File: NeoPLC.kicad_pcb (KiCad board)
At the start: 2 copper layers, 0 parts

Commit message: DI-8 şema ve PCB taslağı: platform kararları kilitlendi, çekirdek/saha yerleşimi GitHub’da.
Birkaç saatlik stabil anlarda origin’e push kuralı eklendi; yerel KiCAD geçmişi ve Konnect önizlemeleri commit dışı bırakıldı.

Co-authored-by: Cursor <cursoragent@cursor.com>
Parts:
- added C1: 10uF, Capacitor_SMD:C_0805_2012Metric, F.Cu at (12.0, 14.0)
- added C2: 100nF, Capacitor_SMD:C_0402_1005Metric, F.Cu at (15.0, 14.0)
- added C3: 10uF, Capacitor_SMD:C_0805_2012Metric, F.Cu at (24.5, 14.0)
- added C4: 100nF, Capacitor_SMD:C_0402_1005Metric, F.Cu at (21.0, 14.0)
- added C5: 100nF, Capacitor_SMD:C_0402_1005Metric, F.Cu at (20.5, 29.5)
- added C6: 100nF, Capacitor_SMD:C_0402_1005Metric, F.Cu at (20.5, 32.0)
- added C7: 100nF, Capacitor_SMD:C_0402_1005Metric, F.Cu at (20.5, 34.5)
- added C8: 15pF, Capacitor_SMD:C_0402_1005Metric, F.Cu at (17.0, 30.0)
- added C9: 15pF, Capacitor_SMD:C_0402_1005Metric, F.Cu at (17.0, 37.0)
- added D1: LED, LED_SMD:LED_0805_2012Metric, F.Cu at (10.0, 42.0)
- added J1: Backplane 2x6, NeoPLC:GoldFinger_2x6_2.54, F.Cu at (37.5, 0.00)
- added J2: DI1-4+COM 3.5mm, Connector_Phoenix_MC:PhoenixContact_MCV_1,5_5-G-3.5_1x05_P3.50mm_Vertical, F.Cu at (21.0, 105.0)
- added J3: DI5-8+COM 3.5mm, Connector_Phoenix_MC:PhoenixContact_MCV_1,5_5-G-3.5_1x05_P3.50mm_Vertical, F.Cu at (68.0, 105.0)
- added J4: SWD, Connector_PinHeader_2.54mm:PinHeader_1x05_P2.54mm_Vertical, F.Cu at (63.0, 22.0)
- added R1: 10k, Resistor_SMD:R_0402_1005Metric, F.Cu at (20.5, 38.5)
- added R10: 3.3k, Resistor_SMD:R_1206_3216Metric, F.Cu at (62.0, 86.0)
- added R11: 3.3k, Resistor_SMD:R_1206_3216Metric, F.Cu at (64.5, 86.0)
- added R12: 10k, Resistor_SMD:R_0402_1005Metric, F.Cu at (11.5, 67.0)
- added R13: 10k, Resistor_SMD:R_0402_1005Metric, F.Cu at (14.0, 67.0)
- added R14: 10k, Resistor_SMD:R_0402_1005Metric, F.Cu at (16.5, 67.0)
- added R15: 10k, Resistor_SMD:R_0402_1005Metric, F.Cu at (19.0, 67.0)
- added R16: 10k, Resistor_SMD:R_0402_1005Metric, F.Cu at (57.0, 67.0)
- added R17: 10k, Resistor_SMD:R_0402_1005Metric, F.Cu at (59.5, 67.0)
- added R18: 10k, Resistor_SMD:R_0402_1005Metric, F.Cu at (62.0, 67.0)
- added R19: 10k, Resistor_SMD:R_0402_1005Metric, F.Cu at (64.5, 67.0)
- added R2: 1k, Resistor_SMD:R_0402_1005Metric, F.Cu at (10.0, 38.5)
- added R3: 1M, Resistor_SMD:R_0402_1005Metric, F.Cu at (13.5, 33.5)
- added R4: 3.3k, Resistor_SMD:R_1206_3216Metric, F.Cu at (11.5, 86.0)
- added R5: 3.3k, Resistor_SMD:R_1206_3216Metric, F.Cu at (14.0, 86.0)
- added R6: 3.3k, Resistor_SMD:R_1206_3216Metric, F.Cu at (16.5, 86.0)
- added R7: 3.3k, Resistor_SMD:R_1206_3216Metric, F.Cu at (19.0, 86.0)
- added R8: 3.3k, Resistor_SMD:R_1206_3216Metric, F.Cu at (57.0, 86.0)
- added R9: 3.3k, Resistor_SMD:R_1206_3216Metric, F.Cu at (59.5, 86.0)
- added U1: STM32G071CBT6, Package_QFP:LQFP-48_7x7mm_P0.5mm, F.Cu at (28.0, 32.0)
- added U2: AP2112K-3.3, Package_TO_SOT_SMD:SOT-23-5, F.Cu at (18.0, 14.0)
- added U3: ISL3178EIBZ, Package_SO:SOIC-8_3.9x4.9mm_P1.27mm, F.Cu at (52.0, 16.0)
- added U4: TLP291-4, Package_SO:SOIC-16_4.55x10.3mm_P1.27mm, F.Cu at (16.0, 74.0)
- added U5: TLP291-4, Package_SO:SOIC-16_4.55x10.3mm_P1.27mm, F.Cu at (61.5, 74.0)
- added Y1: 8MHz, Crystal:Crystal_SMD_3225-4Pin_3.2x2.5mm, F.Cu at (17.0, 33.5)
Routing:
- net +3V3: track 0.00 -> 296.0 mm, vias 0 -> 13
- net /Node Core/MOD_RST#: track 0.00 -> 214.9 mm, vias 0 -> 13
- net /DI Field/FIELD_COM: track 0.00 -> 124.9 mm
- net /DI Field/DI5: track 0.00 -> 83.7 mm, vias 0 -> 12
- net /DI Field/DI6: track 0.00 -> 81.8 mm, vias 0 -> 13
- net /DI Field/DI7: track 0.00 -> 80.0 mm, vias 0 -> 12
- net /DI Field/DI8: track 0.00 -> 78.2 mm, vias 0 -> 11
- net GND: track 0.00 -> 59.4 mm, vias 0 -> 6
- net /DI Field/DI2: track 0.00 -> 55.5 mm, vias 0 -> 8
- net /Node Core/SWDIO: track 0.00 -> 50.0 mm, vias 0 -> 2
- net /DI Field/DI1: track 0.00 -> 48.8 mm, vias 0 -> 10
- net /DI Field/DI4: track 0.00 -> 47.3 mm, vias 0 -> 11
- net /Node Core/SWCLK: track 0.00 -> 47.0 mm, vias 0 -> 2
- net /Node Core/STATUS_LED: track 0.00 -> 43.5 mm, vias 0 -> 5
- net /DI Field/DI3: track 0.00 -> 43.2 mm, vias 0 -> 8
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- added copper zone on F.Cu, net /DI Field/FIELD_COM
- added copper zone on B.Cu, net GND
- added copper zone on F.Cu, net GND
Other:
- board outline added: 75 x 110 mm

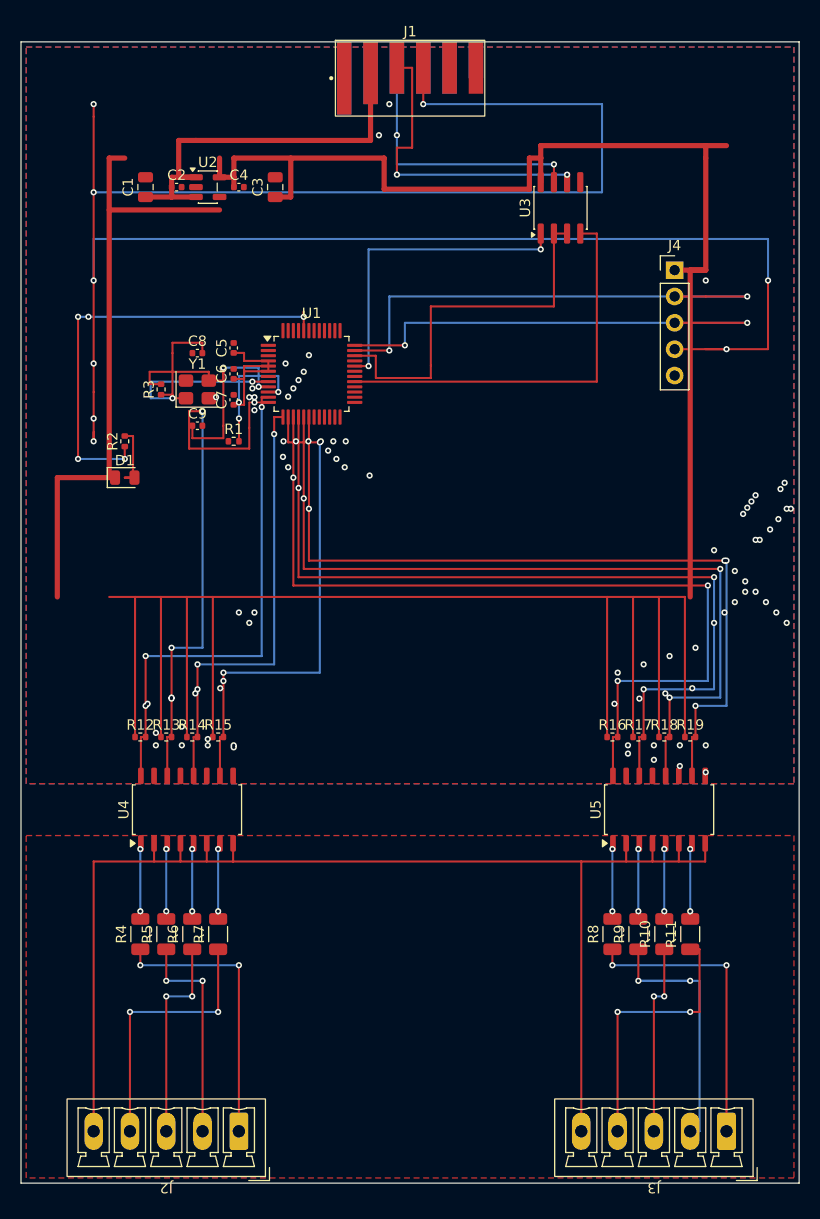
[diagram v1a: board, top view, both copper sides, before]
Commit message: DI6/DI4 last-mile ve J1 +5V arka pad: MCU’ya bakır kapandı, DRC 134→101.
Co-authored-by: Cursor <cursoragent@cursor.com>
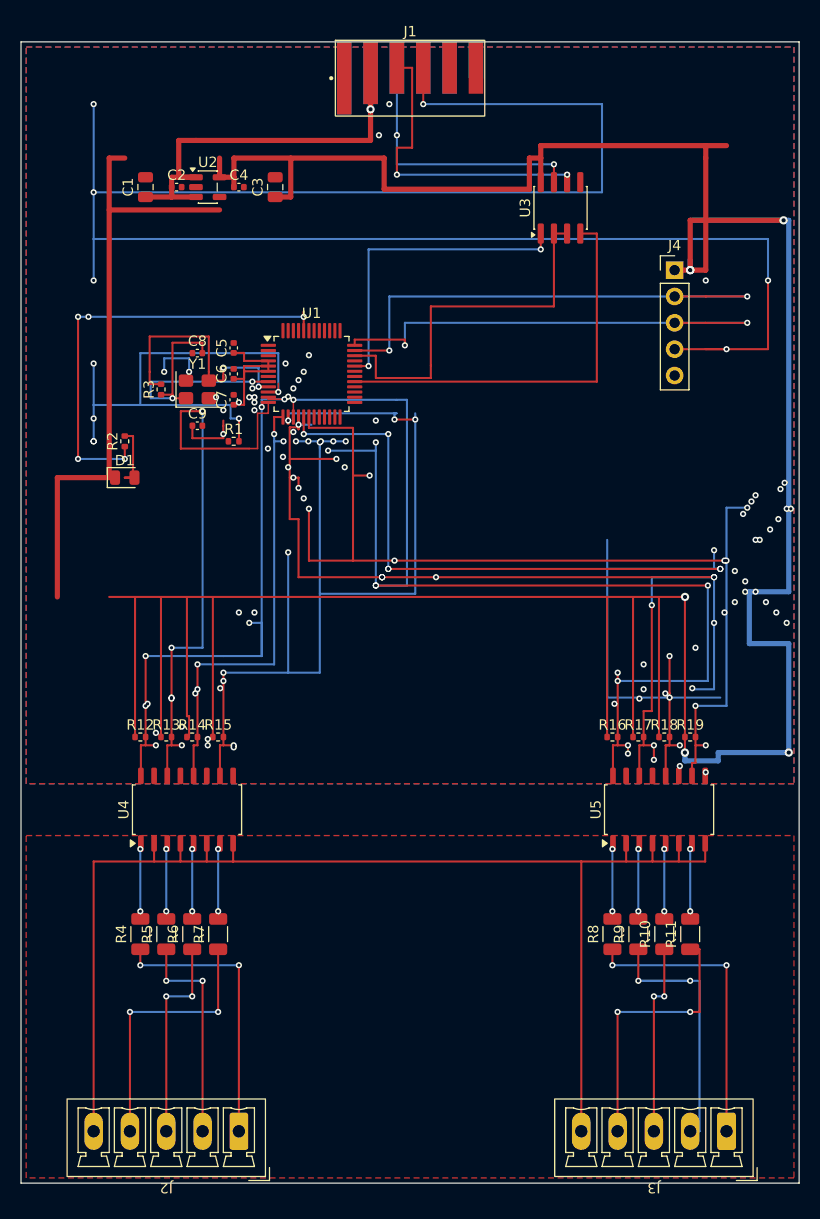
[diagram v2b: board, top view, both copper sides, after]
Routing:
- net +3V3: track 296.0 -> 359.8 mm, vias 13 -> 22
- net /DI Field/DI4: track 47.3 -> 100.8 mm, vias 11 -> 16
- net /DI Field/DI5: track 83.7 -> 114.0 mm, vias 12 -> 14
- net /DI Field/DI7: track 80.0 -> 107.9 mm, vias 12 -> 20
- net /DI Field/DI6: track 81.8 -> 106.9 mm, vias 13 -> 21
- net /DI Field/DI8: track 78.2 -> 97.3 mm, vias 11 -> 10
- net /Node Core/MOD_RST#: track 214.9 -> 230.7 mm, vias 13 -> 14
- net /DI Field/DI1: track 48.8 -> 57.3 mm, vias 10 -> 9
- net GND: track 59.4 -> 64.4 mm, vias 6 -> 8
- net +5V: track 39.3 -> 42.8 mm, vias 0 -> 1
- net /DI Field/DI2: track 55.5 -> 58.1 mm, vias 8 -> 10
- net /Node Core/HSE_OUT: track 28.7 -> 30.8 mm, vias 3 -> 4
- net /Node Core/SWCLK: track 47.0 -> 48.1 mm
- net /DI Field/DI3: track 43.2 -> 44.1 mm

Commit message: +3V3 LDO–MCU köprüsü ve RST/DI ada dikişleri: DRC 98→83.
Co-authored-by: Cursor <cursoragent@cursor.com>
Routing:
- net +3V3: track 359.8 -> 396.7 mm
- net /Node Core/MOD_RST#: track 230.7 -> 248.7 mm, vias 14 -> 13
- net /Node Core/BUS_A: track 30.4 -> 40.1 mm, vias 2 -> 3
- net /Node Core/HSE_OUT: track 30.8 -> 34.7 mm, vias 4 -> 5
- net /DI Field/DI6: track 106.9 -> 110.1 mm
- net /DI Field/DI2: track 58.1 -> 60.1 mm
- net /DI Field/DI7: track 107.9 -> 109.5 mm
- net /DI Field/DI3: track 44.1 -> 45.7 mm
- net /DI Field/DI1: vias 9 -> 8
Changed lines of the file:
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@@
 	)
 	(segment
+		(start 68.8 53.5)
+		(end 68.8 54)
+		(width 0.2)
+		(layer "F.Cu")
+		(net "+3V3")
+	)
+	(segment
 		(start 20.5 32.479999)
 		(end 21.5 32.479999)
@@
 	)
 	(segment
+		(start 71.8 54)
+		(end 71.8 55)
+		(width 0.2)
+		(layer "F.Cu")
+		(net "+3V3")
+	)
+	(segment
 		(start 64.5 17.2)
 		(end 73.5 17.2)
@@
 	)
 	(segment
+		(start 20.52 16)
+		(end 20.52 14)
+		(width 0.5)
+		(layer "F.Cu")
+		(net "+3V3")
+	)
+	(segment
 		(start 66 11.2)
 		(end 66 22)
@@
 	)
 	(segment
+		(start 21.5 16)
+		(end 20.52 16)
+		(width 0.5)
+		(layer "F.Cu")
+		(net "+3V3")
+	)
+	(segment
 		(start 19.1375 13.05)
 		(end 19.1375 11.2)
@@
 	)
 	(segment
+		(start 71.8 55)
+		(end 72.8 55)
+		(width 0.2)
+		(layer "F.Cu")
+		(net "+3V3")
+	)
+	(segment
 		(start 16.2 67)
 		(end 15.99 67)
@@
 	)
 	(segment
+		(start 70.8 54)
+		(end 71.8 54)
+		(width 0.2)
+		(layer "F.Cu")
+		(net "+3V3")
+	)
+	(segment
 		(start 21.5 29.98)
 		(end 21.5 30.75)
@@
 	)
 	(segment
+		(start 21 53.5)
+		(end 21 55)
+		(width 0.5)
+		(layer "F.Cu")
+		(net "+3V3")
+	)
+	(segment
 		(start 63.99 68.5)
 		(end 63.99 67)
@@
 	)
 	(segment
+		(start 34.5 9)
+		(end 34.5 11.2)
+		(width 0.5)
+		(layer "F.Cu")
+		(net "+3V3")
+	)
+	(segment
 		(start 20.52 13.05)
 		(end 20.52 14)
@@
 	)
 	(segment
+		(start 72.8 56)
+		(end 73.8 56)
+		(width 0.2)
+		(layer "F.Cu")
+		(net "+3V3")
+	)
+	(segment
+		(start 21 55)
+		(end 22.5 55)
+		(width 0.5)
+		(layer "F.Cu")
+		(net "+3V3")
+	)
+	(segment
 		(start 66 10)
 		(end 66 11.2)
@@
 	)
 	(segment
+		(start 69.8 53)
+		(end 70.8 53)
+		(width 0.2)
+		(layer "F.Cu")
+		(net "+3V3")
+	)
+	(segment
 		(start 8.5 53.5)
 		(end 64 53.5)
@@
 	)
 	(segment
+		(start 72.8 55)
+		(end 72.8 56)
+		(width 0.2)
+		(layer "F.Cu")
+		(net "+3V3")
+	)
+	(segment
 		(start 66 22)
 		(end 63 22)
@@
 	)
 	(segment
+		(start 70.8 53)
+		(end 70.8 54)
+		(width 0.2)
+		(layer "F.Cu")
+		(net "+3V3")
+	)
+	(segment
 		(start 10.99 53.5)
 		(end 10.99 67)
@@
 	)
 	(segment
+		(start 64 53.5)
+		(end 68.8 53.5)
+		(width 0.2)
+		(layer "F.Cu")
+		(net "+3V3")
+	)
+	(segment
 		(start 23.8375 31.25)
 		(end 23.8375 31.75)
@@
 	)
 	(segment
+		(start 69.8 54)
+		(end 69.8 53)
+		(width 0.2)
+		(layer "F.Cu")
+		(net "+3V3")
+	)
+	(segment
+		(start 21.5 29.98)
+		(end 21.5 16)
+		(width 0.5)
+		(layer "F.Cu")
+		(net "+3V3")
+	)
+	(segment
 		(start 23.8375 30.75)
 		(end 23.8375 31.25)
@@
 	)
 	(segment
+		(start 34.5 11.2)
+		(end 35 11.2)
+		(width 0.5)
+		(layer "F.Cu")
+		(net "+3V3")
+	)
+	(segment
 		(start 64.5 22)
 		(end 64.5 17.2)
@@
 	)
 	(segment
+		(start 68.8 54)
+		(end 69.8 54)
+		(width 0.2)
+		(layer "F.Cu")
+		(net "+3V3")
+	)
+	(segment
 		(start 15.99 65)
 		(end 16.2 65)
@@
 	)
 	(segment
+		(start 14.51 67)
+		(end 14.51 66)
+		(width 0.2)
+		(layer "F.Cu")
+		(net "/DI Field/DI2")
+	)
+	(segment
 		(start 22.8 35.8)
 		(end 23.8375 35.8)
@@
 	)
 	(segment
+		(start 14.51 66)
+		(end 15.5 66)
+		(width 0.2)
+		(layer "F.Cu")
+		(net "/DI Field/DI2")
+	)
+	(segment
 		(start 23.8375 35.8)
 		(end 23.8375 34.75)
@@
 	)
 	(segment
+		(start 19.5 32.65)
+		(end 19.5 36.5)
+		(width 0.2)
+		(layer "F.Cu")
+		(net "/Node Core/HSE_OUT")
+	)
+	(segment
 		(start 19.5 36.5)
 		(end 19.5 37)
@@
 	)
 	(via
+		(at 19.5 35.5)
+		(size 0.6)
+		(drill 0.3)
+		(layers "F.Cu" "B.Cu")
+		(net "/Node Core/HSE_OUT")
+	)
+	(via
 		(at 19.5 37.8)
 		(size 0.6)
@@
 	)
 	(segment
+		(start 25.3 38.5)
+		(end 25.3 40)
+		(width 0.2)
+		(layer "B.Cu")
+		(net "/DI Field/DI3")
+	)
+	(segment
+		(start 25.3 40)
+		(end 25.25 40)
+		(width 0.2)
+		(layer "B.Cu")
+		(net "/DI Field/DI3")
+	)
+	(segment
 		(start 58.325 79)
 		(end 58.325 77.25)
@@
 	)
 	(segment
+		(start 68.8 50.8)
+		(end 68.8 51)
+		(width 0.2)
+		(layer "F.Cu")
+		(net "/DI Field/DI7")
+	)
+	(segment
 		(start 27.25 37.8)
 		(end 27.25 36.1625)
@@
 	)
 	(segment
+		(start 67.4 50.8)
+		(end 68.8 50.8)
+		(width 0.2)
+		(layer "F.Cu")
+		(net "/DI Field/DI7")
+	)
+	(segment
 		(start 62.51 67.8)
 		(end 62.51 67)
@@
 	)
 	(segment
+		(start 60.01 62.4)
+		(end 60.01 60)
+		(width 0.2)
+		(layer "F.Cu")
+		(net "/DI Field/DI6")
+	)
+	(segment
 		(start 25.9 42)
 		(end 26.25 42)
@@
 	)
 	(segment
+		(start 60.01 62.4)
+		(end 60.8 62.4)
+		(width 0.2)
+		(layer "F.Cu")
+		(net "/DI Field/DI6")
+	)
+	(segment
 		(start 60.01 64.5)
 		(end 60.8 64.5)
@@
 	)
 	(via
-		(at 35.5 6)
-		(size 0.6)
-		(drill 0.3)
-		(layers "F.Cu" "B.Cu")
-		(net "/Node Core/MOD_RST#")
-	)
-	(via
 		(at 7 14.5)
 		(size 0.6)
@@
 	)
 	(segment
+		(start 66 23)
+		(end 66 19)
+		(width 0.2)
+		(layer "B.Cu")
+		(net "/Node Core/MOD_RST#")
+	)
+	(segment
 		(start 7 23)
 		(end 7 19)
@@
 	)
 	(segment
+		(start 4 31)
+		(end 7 31)
+		(width 0.2)
+		(layer "B.Cu")
+		(net "/Node Core/MOD_RST#")
+	)
+	(segment
 		(start 20.2 36.3)
 		(end 21.01 36.3)
@@
 	)
 	(segment
+		(start 4 23)
+		(end 4 31)
+		(width 0.2)
+		(layer "B.Cu")
+		(net "/Node Core/MOD_RST#")
+	)
+	(segment
+		(start 7 23)
+		(end 4 23)
+		(width 0.2)
+		(layer "B.Cu")
+		(net "/Node Core/MOD_RST#")
+	)
+	(segment
 		(start 7 19)
 		(end 72 19)
@@
 	)
 	(via
-		(at 19.5 35.5)
-		(size 0.6)
-		(drill 0.3)
-		(layers "F.Cu" "B.Cu")
-		(net "/DI Field/DI1")
-	)
-	(via
 		(at 23.2 35.2)
 		(size 0.6)
@@
 	)
 	(via
+		(at 35.5 6)
+		(size 0.6)
+		(drill 0.3)
+		(layers "F.Cu" "B.Cu")
+		(net "/Node Core/BUS_A")
+	)
+	(via
 		(at 36.23 12.8)
 		(size 0.6)
@@
 		(width 0.2)
 		(layer "B.Cu")
+		(net "/Node Core/BUS_A")
+	)
+	(segment
+		(start 35.5 6)
+		(end 35.5 12.5)
+		(width 0.2)
+		(layer "B.Cu")
+		(net "/Node Core/BUS_A")
+	)
+	(segment
+		(start 35.5 12.5)
+		(end 38.77 12.5)
+		(width 0.2)
+		(layer "B.Cu")

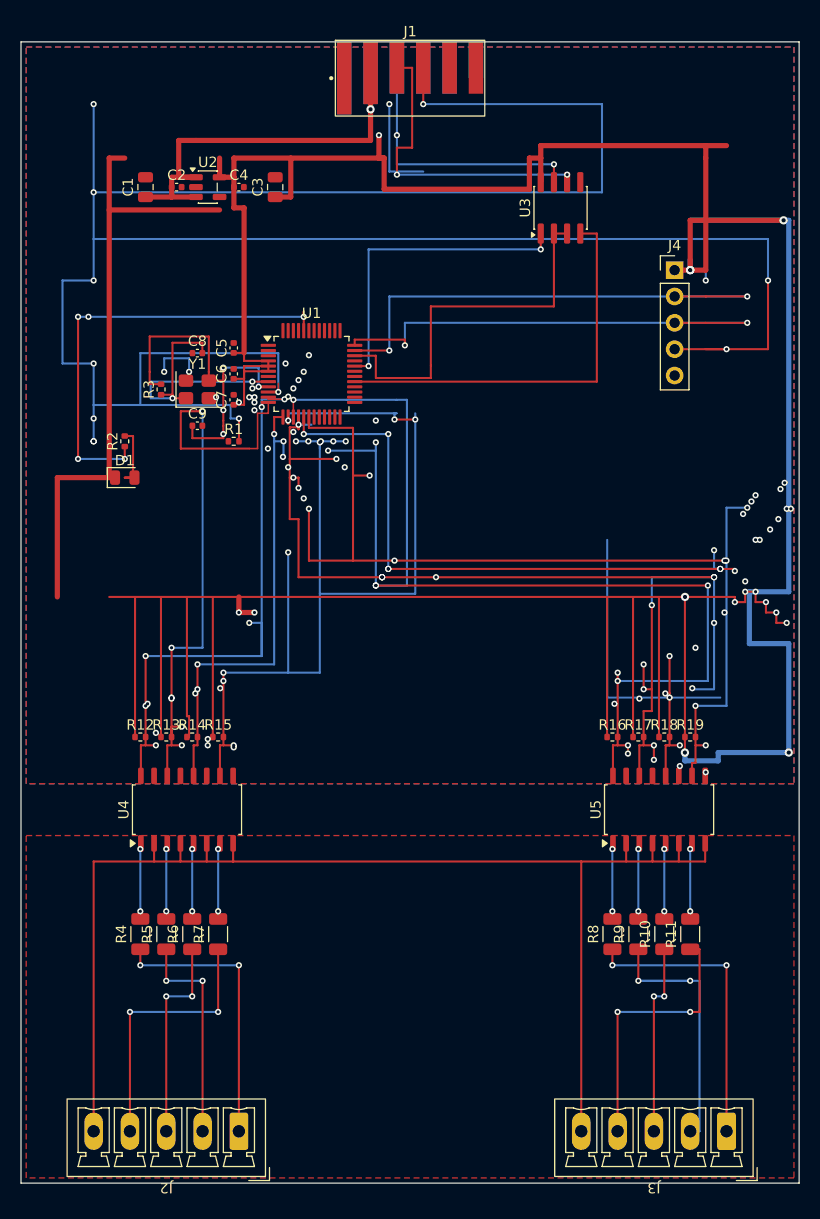
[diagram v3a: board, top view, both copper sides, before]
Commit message: DI8 ada dikişleri, GND via’lar ve SWDIO/STATUS jog: DRC 81→74.
Pad–pull-up netleri kapalı; silinemeyen via kısa devreleri ve J1 gold-finger kenar boşluğu kaldı.

Co-authored-by: Cursor <cursoragent@cursor.com>
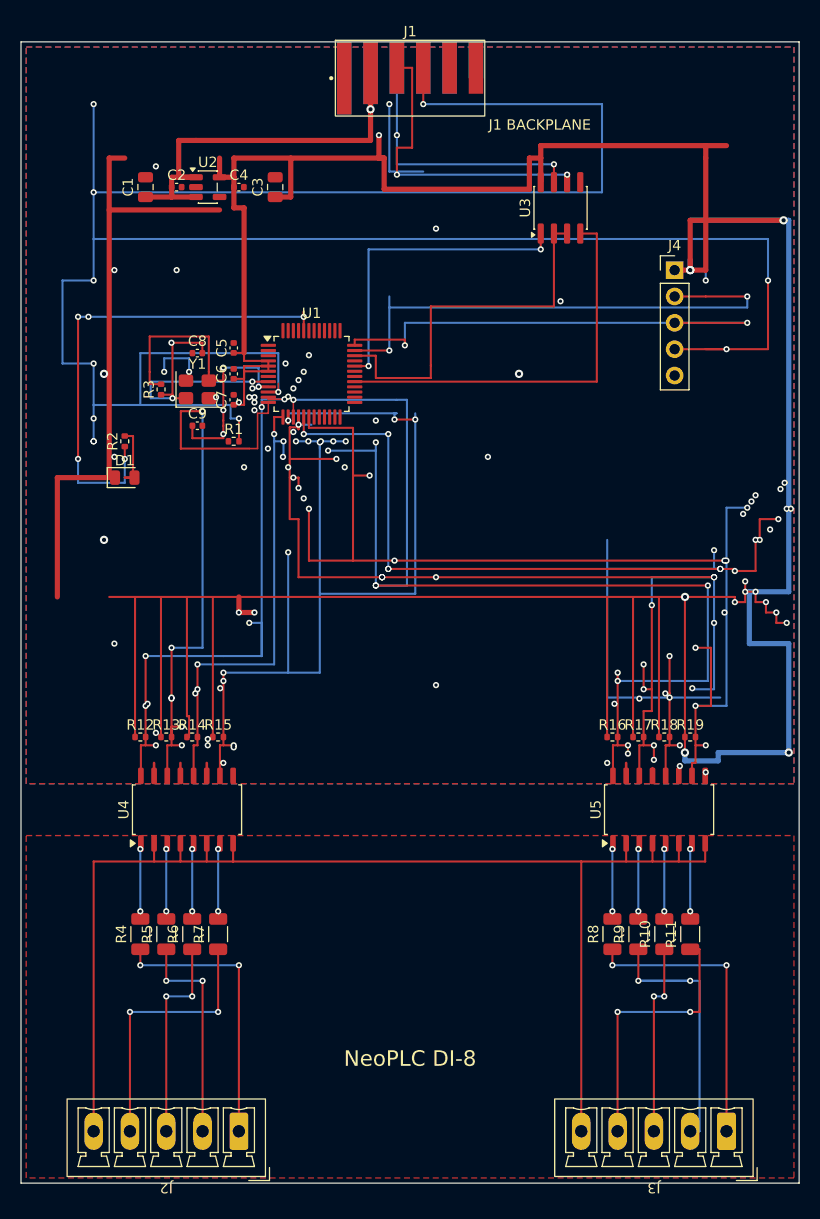
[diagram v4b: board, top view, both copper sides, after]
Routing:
- net /DI Field/DI7: track 109.5 -> 118.7 mm
- net /DI Field/DI8: track 97.3 -> 105.9 mm
- net GND: track 64.4 -> 71.5 mm, vias 8 -> 21
- net /Node Core/STATUS_LED: track 43.5 -> 48.1 mm
- net /Node Core/SWDIO: track 50.0 -> 51.1 mm
- net +3V3: track 396.7 -> 397.6 mm, vias 22 -> 23
- net /Node Core/HSE_OUT: track 34.7 -> 35.4 mm
- net /Node Core/HSE_IN: vias 2 -> 3
- net /DI Field/DI5: vias 14 -> 13
- net /DI Field/DI4: vias 16 -> 17
- net /DI Field/DI2: vias 10 -> 11
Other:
- board text added: "J1 BACKPLANE"
- board text added: "NeoPLC DI-8"
